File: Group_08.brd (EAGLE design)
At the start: 55.9 x 74.9 mm, 29 parts, among them J1 POWER_JACKPTH_LOCK, U1 +12v, U3 TCA9546ATSSOP, U4 TMUX1208

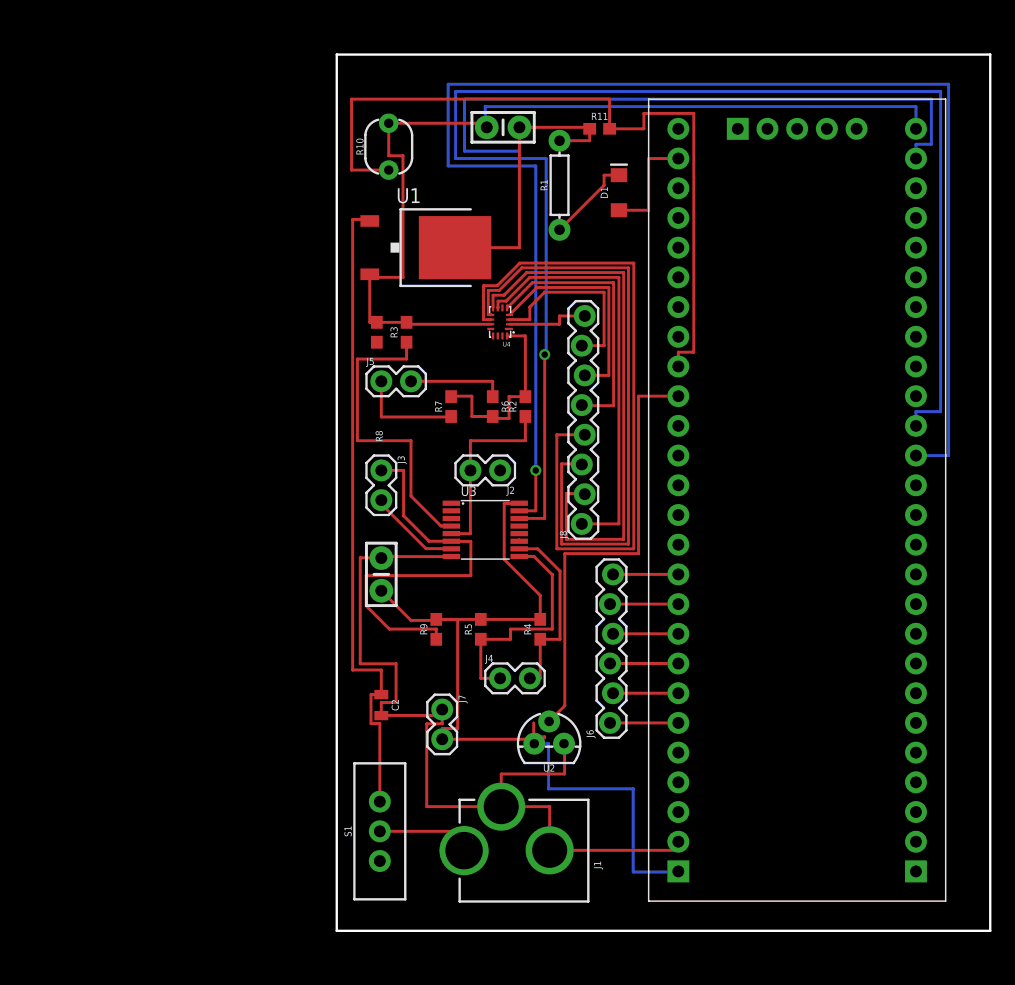
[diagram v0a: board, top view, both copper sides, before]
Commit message: Deleted original prototypes and updated file names
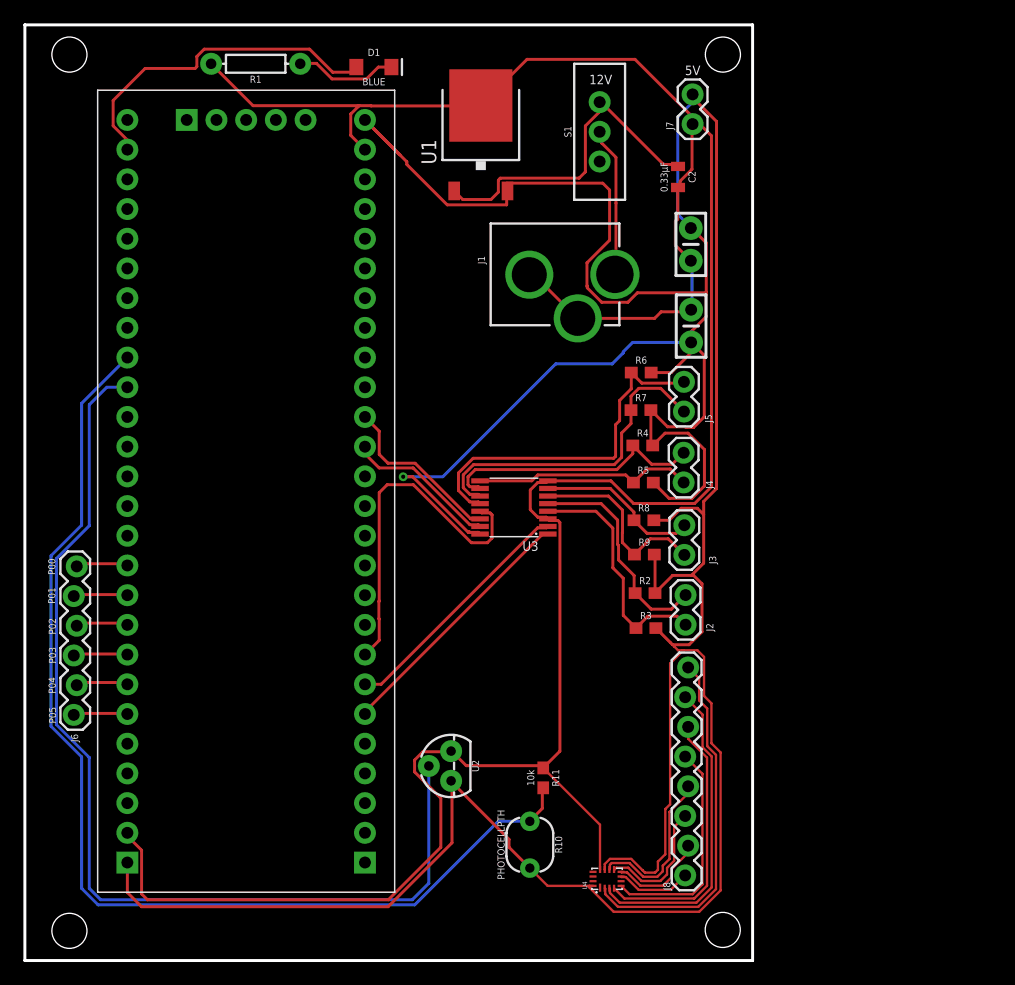
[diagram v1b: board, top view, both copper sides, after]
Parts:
- moved S1 62.7 mm to (49.1, 70.9)
- moved R10 60.9 mm to (43.2, 9.91), turned to 270 degrees
- moved R11 55.7 mm to (44.3, 15.6), turned to 270 degrees
- moved J7 54.5 mm to (57.1, 71.5), turned to 90 degrees
- moved C2 51.8 mm to (55.9, 67.0)
- moved J1 51.5 mm to (36.6, 58.7), turned to 270 degrees
- moved U4 48.5 mm to (49.8, 6.99), turned to 90 degrees
- moved CY8CKIT059-TARGET 47.1 mm to (20.2, 38.9)
- moved J6 45.9 mm to (4.18, 21.0)
- moved C3 38.7 mm to (56.9, 61.2), turned to 270 degrees
- moved R3 32.5 mm to (53.1, 28.4), turned to 0 degrees
- moved J8 31.3 mm to (56.6, 7.28)
- moved R1 28.0 mm to (19.7, 76.7), turned to 180 degrees
- moved R8 27.9 mm to (52.9, 37.6), turned to 0 degrees
- moved J3 26.9 mm to (56.4, 34.7), turned to 90 degrees
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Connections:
- removed net IDC_SDA_0: R3.1, U3.4
- net I2C_SDA_0: now also R3.1, U3.4
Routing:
- net 5V: track 174.4 -> 330.9 mm, vias 0 -> 1
- net I2C_SDA: track 122.7 -> 13.0 mm, vias 1 -> 0
- net I2C_SCL: track 118.7 -> 14.6 mm, vias 1 -> 0
- net GND: track 163.2 -> 226.0 mm
- net TEMP_OUT: track 38.1 -> 87.6 mm
- net N$13: track 60.3 -> 13.9 mm
- net N$12: track 53.0 -> 10.9 mm
- net N$11: track 46.3 -> 8.39 mm
- net I2C_A2: track 0.00 -> 29.7 mm
- net N$10: track 36.0 -> 6.46 mm
- net PHOTO_OUT: track 65.3 -> 94.4 mm
- net 12V: track 55.5 -> 28.6 mm
- net IDC_SDA_0: track 26.4 -> 0.00 mm
- net N$18: track 7.15 -> 31.0 mm
- net I2C_SCL_3: track 8.29 -> 30.5 mm
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- added copper zone on layer 16, net 5V
- added copper zone on layer 1, net GND
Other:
- board size 55.9 x 74.9 mm -> 62.2 x 80 mm
- board text added: "12V"
- board text added: "5V"
- board text added: "P00"
- board text added: "P01"
- board text added: "P02"
- board text added: "P03"
- board text added: "P04"
- board text added: "P05"

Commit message: minor adjustments at wire positioning and silkscreen
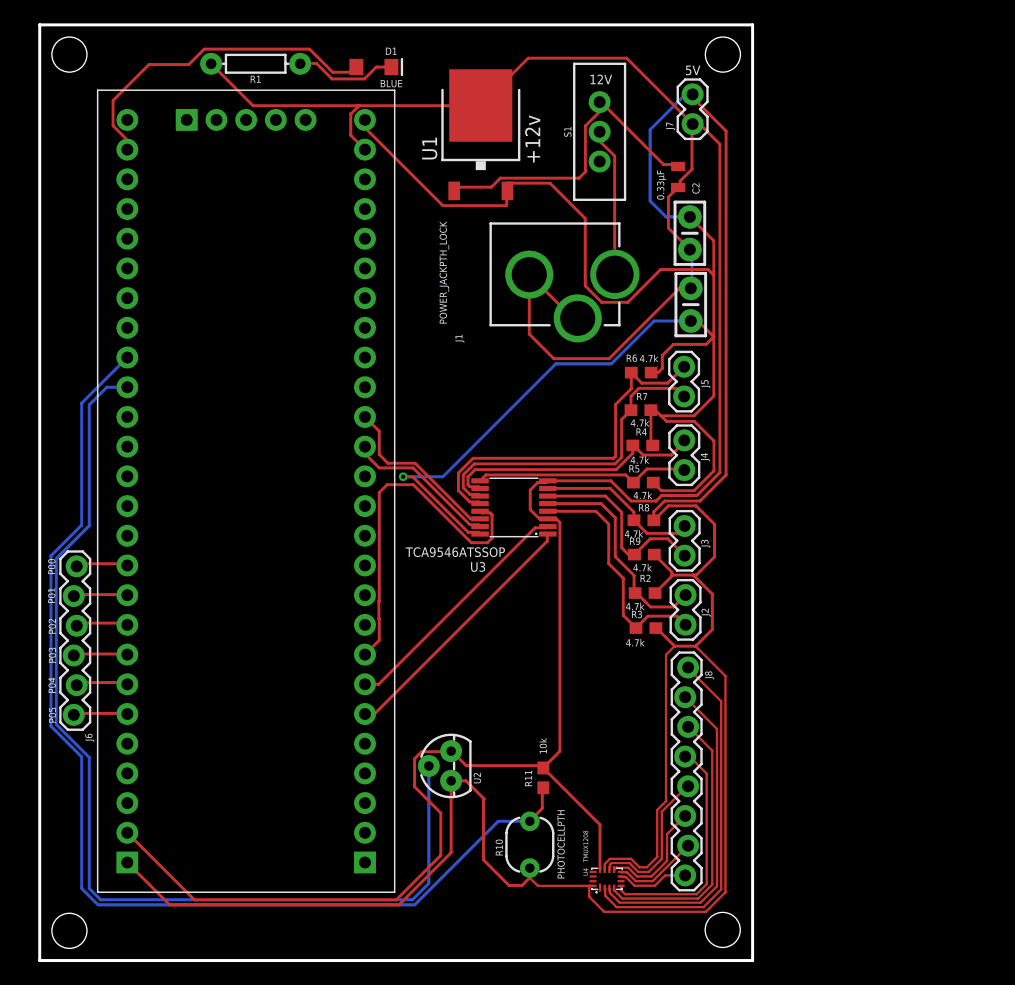
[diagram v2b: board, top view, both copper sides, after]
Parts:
- moved C1 1.83 mm to (56.9, 56.1)
- moved J5 1.29 mm to (56.4, 48.2)
- moved J4 1.06 mm to (56.4, 41.9)
- moved C3 0.95 mm to (56.9, 62.2)
- moved J3 0.07 mm to (56.4, 34.6)
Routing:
- net GND: track 226.0 -> 235.3 mm
- net 5V: track 330.9 -> 336.7 mm
- net 12V: track 28.6 -> 27.4 mm
- net N$11: track 8.39 -> 7.31 mm
- net N$12: track 10.9 -> 9.93 mm
- net N$13: track 13.9 -> 12.9 mm
- net N$14: track 19.1 -> 20.1 mm
- net N$18: track 31.0 -> 31.8 mm
- net N$16: track 23.0 -> 23.7 mm
- net N$17: track 27.2 -> 27.8 mm
- net I2C_SCL_3: track 30.5 -> 31.0 mm
- net I2C_SDA_3: track 28.2 -> 27.7 mm
- net N$26: track 28.8 -> 28.3 mm
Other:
- board size 62.2 x 80 mm -> 61 x 80 mm

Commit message: Updated schematics connections
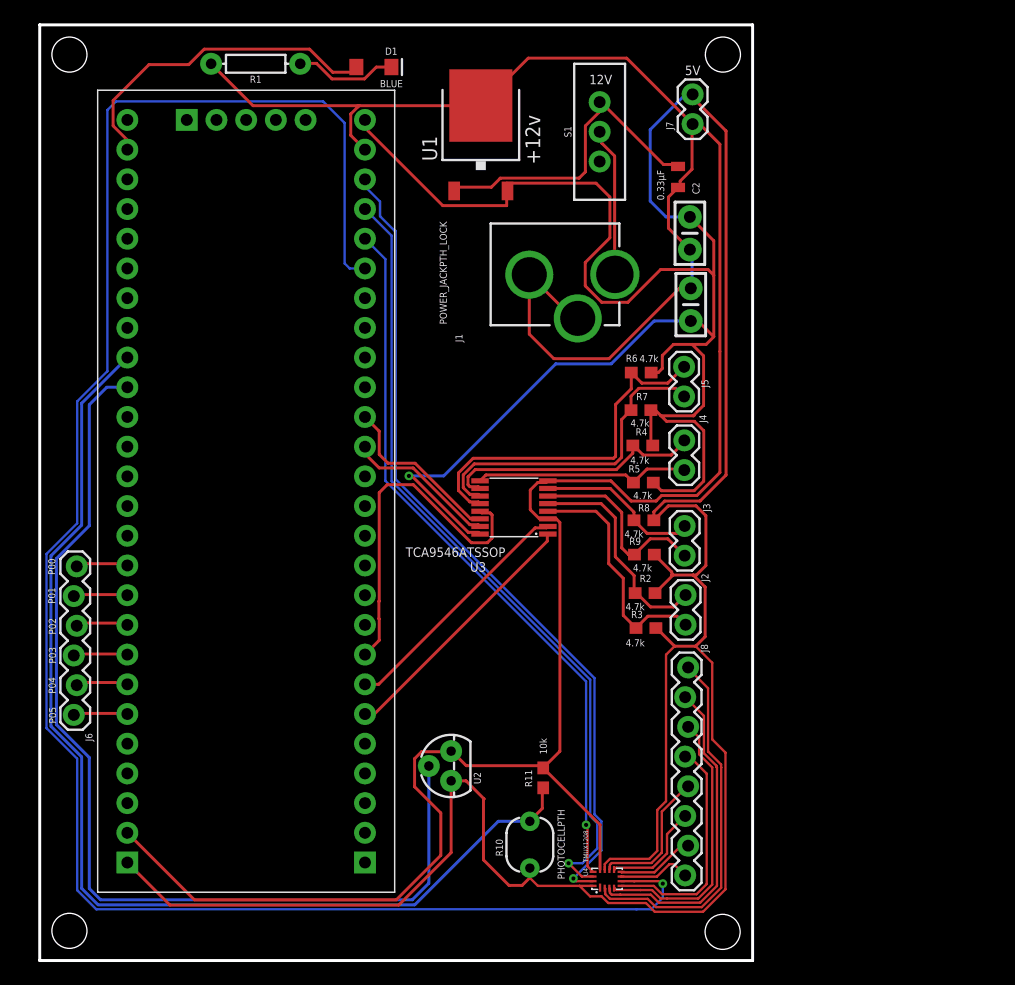
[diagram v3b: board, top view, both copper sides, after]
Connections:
- removed net MUX_A0/1.3C: U4.15
- removed net MUX_A0/2.3C: CY8CKIT059-TARGET.24
- removed net MUX_A1/1.4C: U4.14
- removed net MUX_A1/2.3C: CY8CKIT059-TARGET.23
- removed net MUX_A2/1.4C: U4.13
- removed net MUX_A2/2.3C: CY8CKIT059-TARGET.22
- removed net MUX_OUT/1.4C: U4.6
- removed net MUX_OUT/2.5C: CY8CKIT059-TARGET.21
- new net MUX_A0: CY8CKIT059-TARGET.24, U4.15
- new net MUX_A1: CY8CKIT059-TARGET.23, U4.14
- new net MUX_A2: CY8CKIT059-TARGET.22, U4.13
- new net MUX_OUT: CY8CKIT059-TARGET.21, U4.6
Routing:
- net MUX_OUT: track 0.00 -> 161.3 mm, vias 0 -> 1
- net MUX_A0: track 0.00 -> 71.0 mm, vias 0 -> 1
- net MUX_A1: track 0.00 -> 68.4 mm, vias 0 -> 1
- net MUX_A2: track 0.00 -> 62.2 mm, vias 0 -> 1
- net N$12: track 9.93 -> 8.94 mm
- net N$13: track 12.9 -> 11.9 mm
- net N$11: track 7.31 -> 6.70 mm
